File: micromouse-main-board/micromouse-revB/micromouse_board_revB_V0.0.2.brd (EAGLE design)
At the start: 128.4 x 85.5 mm, 110 parts, among them IC1 LM321MFX, J3 HTSS-103-XX-XX-D, J5 HTSS-103-XX-XX-D, J6 HTSS-102-XX-XX-D, U2 DRV8848PWPR, U3 ACS712ELCTR-20A-T, U6 MPU-6000, X1 RASPI_GPIO_B+#_PIN

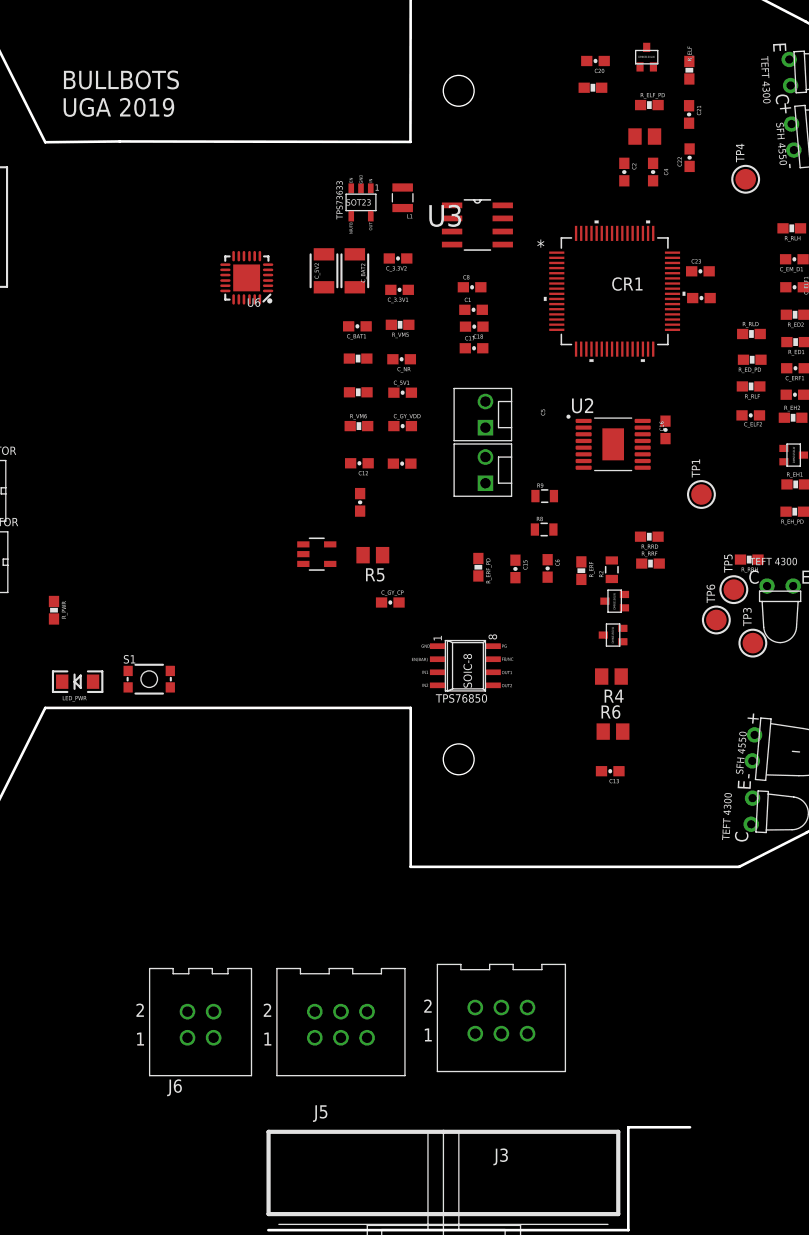
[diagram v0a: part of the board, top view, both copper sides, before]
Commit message: power reg. added placement done
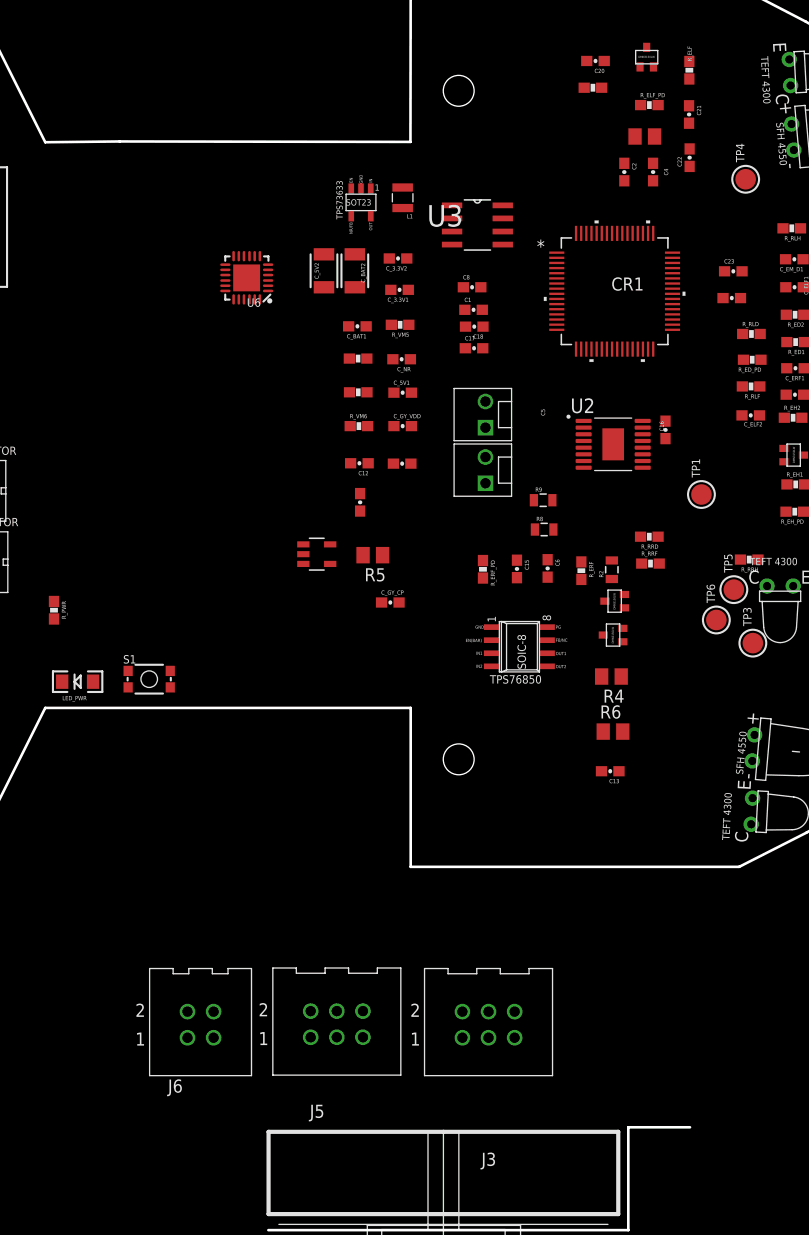
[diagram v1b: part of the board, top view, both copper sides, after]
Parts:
- moved U$4 5.57 mm to (44.6, 12.6)
- moved C23 3.20 mm to (65.5, 49.1)
- moved C7 2.95 mm to (65.3, 46.5)
- moved J3 1.31 mm to (41.6, -24.1)
- moved R_ERF_PD 0.49 mm to (41.1, 20.1)
- moved R9 0.43 mm to (47.0, 26.8)
- moved J5 0.40 mm to (26.9, -24.1)
- moved C15 0.15 mm to (44.4, 20.2)
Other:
- board text removed: "BULLBOTS UGA 2019"
